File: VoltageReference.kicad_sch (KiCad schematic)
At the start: 1 part

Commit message: finish some unconnect pins, draw edge cut board
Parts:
- RV2: footprint IVS_FOOTPRINTS:Potentiometer_Bourns_TC33X_Vertical -> SpiritBoi_Footprint_Library:Potentiometer-Vert-SMD-3P-Bourns_TC33X
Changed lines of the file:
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@@
 			)
 		)
-		(property "Footprint" "IVS_FOOTPRINTS:Potentiometer_Bourns_TC33X_Vertical"
+		(property "Footprint" "SpiritBoi_Footprint_Library:Potentiometer-Vert-SMD-3P-Bourns_TC33X"
 			(at 81.915 95.25 0)
 			(effects

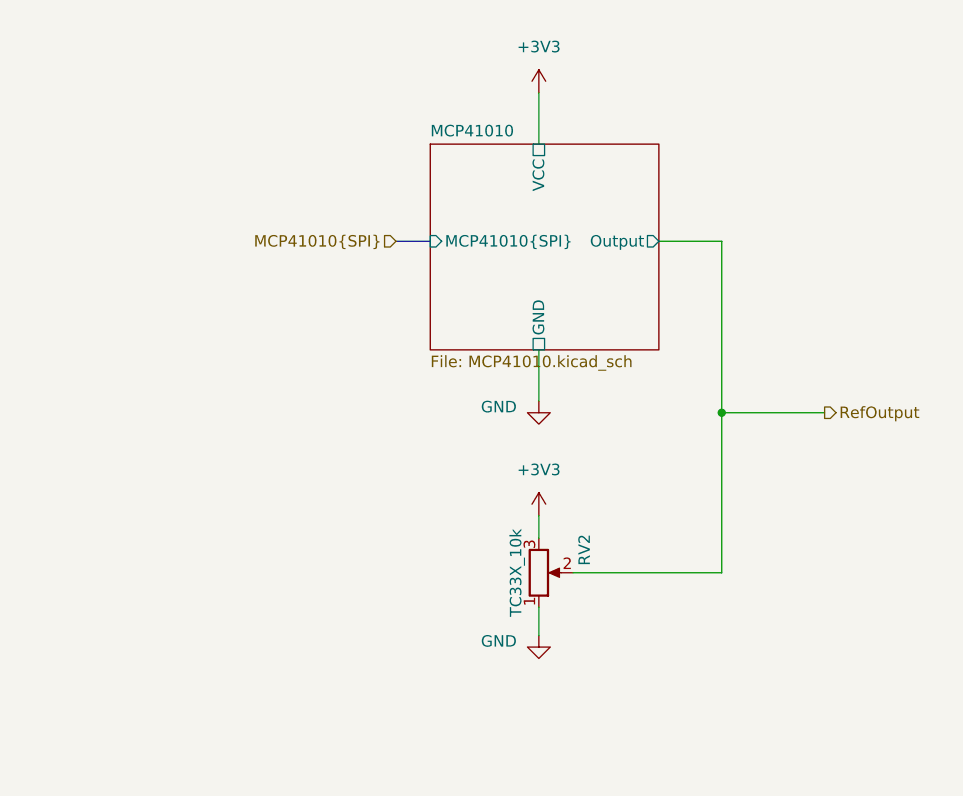
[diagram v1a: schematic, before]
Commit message: Add LORA, SDcard and Volt to 4_20mA scheamtic
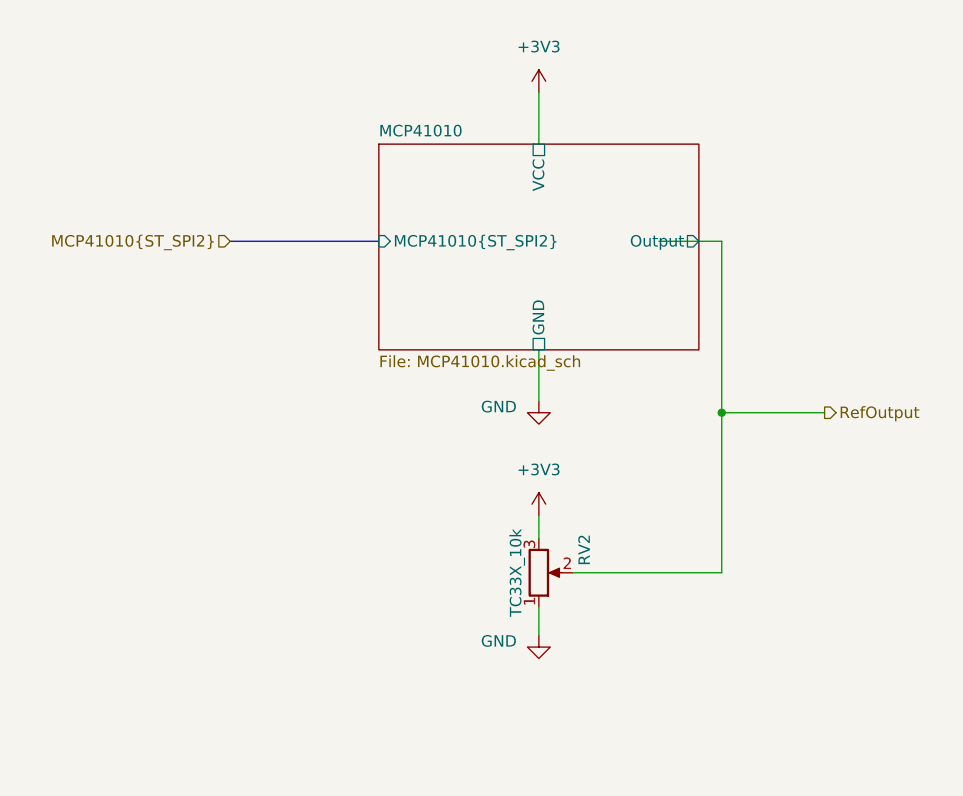
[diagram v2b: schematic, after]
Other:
- sheet MCP41010 ports: added MCP41010{ST_SPI2}; removed MCP41010{SPI}
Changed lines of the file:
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@@
 	(bus
 		(pts
-			(xy 66.04 58.42) (xy 69.85 58.42)
+			(xy 47.625 58.42) (xy 64.135 58.42)
 		)
 		(stroke
@@
 		)
 	)
-	(hierarchical_label "MCP41010{SPI}"
+	(hierarchical_label "MCP41010{ST_SPI2}"
 		(shape input)
-		(at 66.04 58.42 180)
+		(at 47.625 58.42 180)
 		(fields_autoplaced yes)
 		(effects
@@
 		(on_board yes)
 		(dnp no)
-		(property "Reference" "#PWR0141"
+		(property "Reference" "#PWR0112"
 			(at 81.915 108.585 0)
 			(effects
@@
 			(project "DongTamV2"
 				(path "/2303d546-b88a-4ab0-aee1-26e3b32ac9d7/c44414d4-f62b-4b90-ad16-4c8725291991"
-					(reference "#PWR0141")
+					(reference "#PWR0112")
 					(unit 1)
 				)
@@
 		(dnp no)
 		(fields_autoplaced yes)
-		(property "Reference" "#PWR0140"
+		(property "Reference" "#PWR0111"
 			(at 81.915 92.71 0)
 			(effects
@@
 			(project "DongTamV2"
 				(path "/2303d546-b88a-4ab0-aee1-26e3b32ac9d7/c44414d4-f62b-4b90-ad16-4c8725291991"
-					(reference "#PWR0140")
+					(reference "#PWR0111")
 					(unit 1)
 				)
@@
 		(on_board yes)
 		(dnp no)
-		(property "Reference" "#PWR0121"
+		(property "Reference" "#PWR0110"
 			(at 81.915 82.55 0)
 			(effects
@@
 			(project "DongTamV2"
 				(path "/2303d546-b88a-4ab0-aee1-26e3b32ac9d7/c44414d4-f62b-4b90-ad16-4c8725291991"
-					(reference "#PWR0121")
+					(reference "#PWR0110")
 					(unit 1)
 				)
@@
 		(dnp no)
 		(fields_autoplaced yes)
-		(property "Reference" "#PWR0122"
+		(property "Reference" "#PWR0109"
 			(at 81.915 45.72 0)
 			(effects
@@
 			(project "DongTamV2"
 				(path "/2303d546-b88a-4ab0-aee1-26e3b32ac9d7/c44414d4-f62b-4b90-ad16-4c8725291991"
-					(reference "#PWR0122")
+					(reference "#PWR0109")
 					(unit 1)
 				)
@@
 	)
 	(sheet
-		(at 69.85 47.625)
-		(size 25.4 22.86)
+		(at 64.135 47.625)
+		(size 35.56 22.86)
 		(fields_autoplaced yes)
 		(stroke
@@
 		)
 		(property "Sheetname" "MCP41010"
-			(at 69.85 46.9134 0)
+			(at 64.135 46.9134 0)
 			(effects
 				(font
@@
 		)
 		(property "Sheetfile" "MCP41010.kicad_sch"
-			(at 69.85 71.0696 0)
+			(at 64.135 71.0696 0)
 			(effects
 				(font
@@
 		)
 		(pin "Output" output
-			(at 95.25 58.42 0)
+			(at 99.695 58.42 0)
 			(effects
 				(font
@@
 			)
 		)
-		(pin "MCP41010{SPI}" input
-			(at 69.85 58.42 180)
-			(effects
-				(font
+		(pin "MCP41010{ST_SPI2}" input
+			(at 64.135 58.42 180)
+			(effects
+				(font

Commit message: layout p1
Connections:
- net +3V3 renamed +3.3V
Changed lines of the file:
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@@
+	)
+	(symbol
+		(lib_id "power:+3.3V")
+		(at 81.915 88.9 0)
+		(unit 1)
+		(exclude_from_sim no)
+		(in_bom yes)
+		(on_board yes)
+		(dnp no)
+		(fields_autoplaced yes)
+		(property "Reference" "#PWR0109"
+			(at 81.915 92.71 0)
+			(effects
+				(font
+					(size 1.27 1.27)
+				)
+				(hide yes)
+			)
+		)
+		(property "Value" "+3.3V"
+			(at 81.915 83.82 0)
+			(effects
+				(font
+					(size 1.27 1.27)
+				)
+			)
+		)
+		(property "Footprint" ""
+			(at 81.915 88.9 0)
+			(effects
+				(font
+					(size 1.27 1.27)
+				)
+				(hide yes)
+			)
+		)
+		(property "Datasheet" ""
+			(at 81.915 88.9 0)
+			(effects
+				(font
+					(size 1.27 1.27)
+				)
+				(hide yes)
+			)
+		)
+		(property "Description" "Power symbol creates a global label with name \"+3.3V\""
+			(at 81.915 88.9 0)
+			(effects
+				(font
+					(size 1.27 1.27)
+				)
+				(hide yes)
+			)
+		)
+		(pin "1"
+		)
+		(instances
+			(project "DongTamV2"
+				(path "/2303d546-b88a-4ab0-aee1-26e3b32ac9d7/c44414d4-f62b-4b90-ad16-4c8725291991"
+					(reference "#PWR0109")
+					(unit 1)
+				)
+			)
+		)
 	)
 	(symbol
@@
 	)
 	(symbol
-		(lib_id "power:+3V3")
-		(at 81.915 88.9 0)
-		(mirror y)
-		(unit 1)
-		(exclude_from_sim no)
-		(in_bom yes)
-		(on_board yes)
-		(dnp no)
-		(fields_autoplaced yes)
-		(property "Reference" "#PWR0111"
-			(at 81.915 92.71 0)
-			(effects
-				(font
-					(size 1.27 1.27)
-				)
-				(hide yes)
-			)
-		)
-		(property "Value" "+3V3"
-			(at 81.915 83.82 0)
-			(effects
-				(font
-					(size 1.27 1.27)
-				)
-			)
-		)
-		(property "Footprint" ""
-			(at 81.915 88.9 0)
-			(effects
-				(font
-					(size 1.27 1.27)
-				)
-				(hide yes)
-			)
-		)
-		(property "Datasheet" ""
-			(at 81.915 88.9 0)
-			(effects
-				(font
-					(size 1.27 1.27)
-				)
-				(hide yes)
-			)
-		)
-		(property "Description" ""
-			(at 81.915 88.9 0)
-			(effects
-				(font
-					(size 1.27 1.27)
-				)
-				(hide yes)
-			)
-		)
-		(pin "1"
-		)
-		(instances
-			(project "DongTamV2"
-				(path "/2303d546-b88a-4ab0-aee1-26e3b32ac9d7/c44414d4-f62b-4b90-ad16-4c8725291991"
-					(reference "#PWR0111")
-					(unit 1)
-				)
-			)
-		)
-	)
-	(symbol
 		(lib_id "power:GND")
 		(at 81.915 76.2 0)
@@
 	)
 	(symbol
+		(lib_id "power:+3.3V")
+		(at 81.915 41.91 0)
+		(unit 1)
+		(exclude_from_sim no)
+		(in_bom yes)
+		(on_board yes)
+		(dnp no)
+		(fields_autoplaced yes)
+		(property "Reference" "#PWR048"
+			(at 81.915 45.72 0)
+			(effects
+				(font
+					(size 1.27 1.27)
+				)
+				(hide yes)
+			)
+		)
+		(property "Value" "+3.3V"
+			(at 81.915 36.83 0)
+			(effects
+				(font
+					(size 1.27 1.27)
+				)
+			)
+		)
+		(property "Footprint" ""
+			(at 81.915 41.91 0)
+			(effects
+				(font
+					(size 1.27 1.27)
+				)
+				(hide yes)
+			)
+		)
+		(property "Datasheet" ""
+			(at 81.915 41.91 0)
+			(effects
+				(font
+					(size 1.27 1.27)
+				)
+				(hide yes)
+			)
+		)
+		(property "Description" "Power symbol creates a global label with name \"+3.3V\""
+			(at 81.915 41.91 0)
+			(effects
+				(font
+					(size 1.27 1.27)
+				)
+				(hide yes)
+			)
+		)
+		(pin "1"
+		)
+		(instances
+			(project "DongTamV2"
+				(path "/2303d546-b88a-4ab0-aee1-26e3b32ac9d7/c44414d4-f62b-4b90-ad16-4c8725291991"
+					(reference "#PWR048")
+					(unit 1)
+				)
+			)
+		)
+	)
+	(symbol
 		(lib_id "Device:R_Potentiometer")
 		(at 81.915 95.25 0)
@@
 					(unit 1)
 				)
-			)
-		)
-	)
-	(symbol
-		(lib_id "power:+3V3")
-		(at 81.915 41.91 0)
-		(mirror y)
-		(unit 1)
-		(exclude_from_sim no)
-		(in_bom yes)
-		(on_board yes)
-		(dnp no)
-		(fields_autoplaced yes)
-		(property "Reference" "#PWR0109"
-			(at 81.915 45.72 0)
-			(effects
-				(font
-					(size 1.27 1.27)
-				)
-				(hide yes)
-			)
-		)
-		(property "Value" "+3V3"
-			(at 81.915 36.83 0)
-			(effects
-				(font
-					(size 1.27 1.27)
-				)
-			)
-		)
-		(property "Footprint" ""
-			(at 81.915 41.91 0)
-			(effects
-				(font
-					(size 1.27 1.27)
-				)
-				(hide yes)
-			)
-		)
-		(property "Datasheet" ""
-			(at 81.915 41.91 0)
-			(effects
-				(font
-					(size 1.27 1.27)
-				)
-				(hide yes)
-			)
-		)
-		(property "Description" ""
-			(at 81.915 41.91 0)
-			(effects
-				(font
-					(size 1.27 1.27)
-				)
-				(hide yes)
-			)
-		)
-		(pin "1"
-		)
-		(instances
-			(project "DongTamV2"
-				(path "/2303d546-b88a-4ab0-aee1-26e3b32ac9d7/c44414d4-f62b-4b90-ad16-4c8725291991"
-					(reference "#PWR0109")
-					(unit 1)
-				)

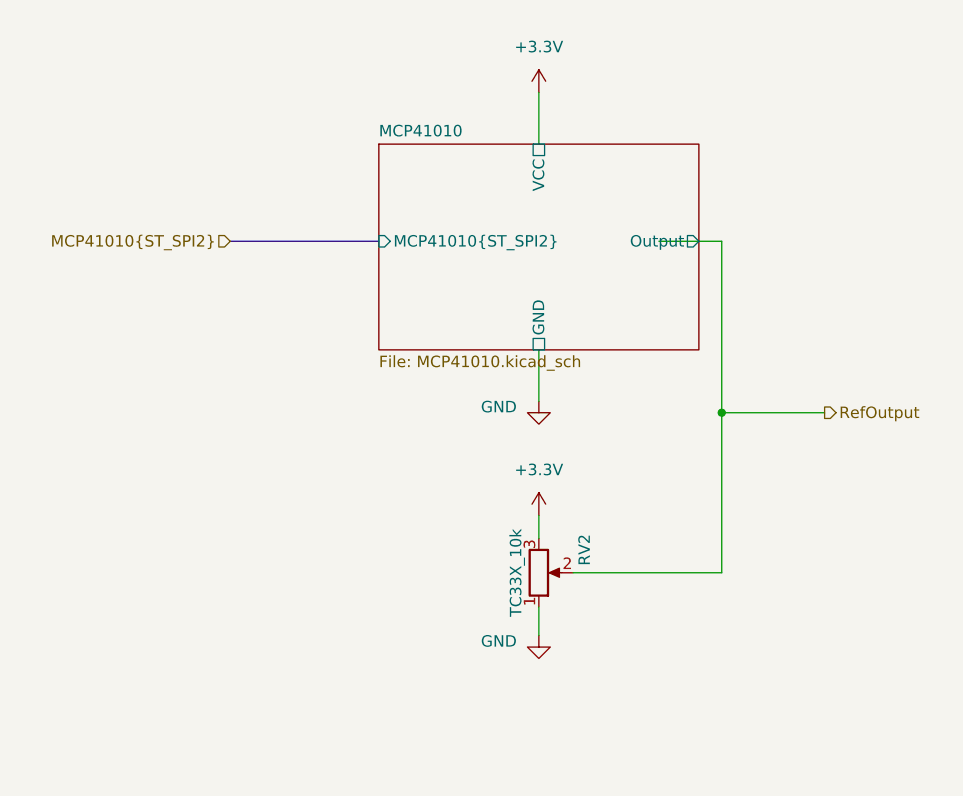
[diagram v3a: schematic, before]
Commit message: Layout p2, fix Analog VCC and GND for opamp circuit
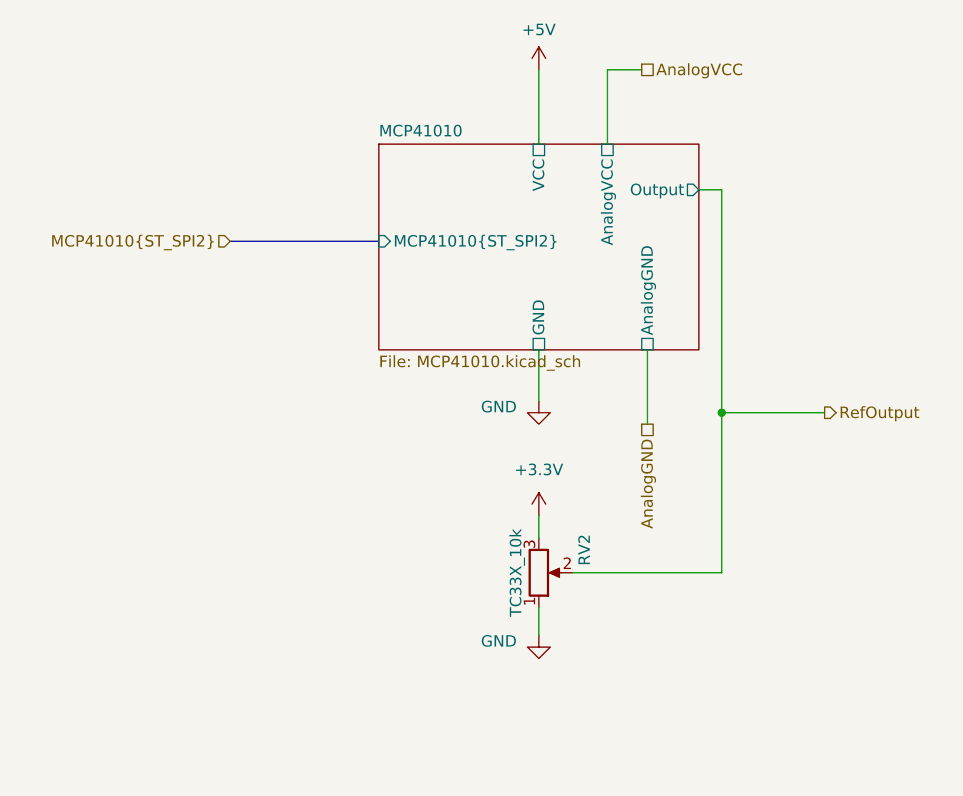
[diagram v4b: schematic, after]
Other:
- sheet MCP41010 ports: added AnalogGND, AnalogVCC; removed none
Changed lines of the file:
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@@
+	(wire
+		(pts
+			(xy 81.915 39.37) (xy 81.915 47.625)
+		)
+		(stroke
+			(width 0)
+			(type default)
+		)
+	)
 	(wire
 		(pts
@@
 	(wire
 		(pts
-			(xy 102.235 77.47) (xy 102.235 58.42)
+			(xy 102.235 77.47) (xy 102.235 52.705)
 		)
 		(stroke
@@
 	(wire
 		(pts
-			(xy 102.235 58.42) (xy 95.25 58.42)
+			(xy 93.345 39.37) (xy 89.535 39.37)
 		)
 		(stroke
@@
 	(wire
 		(pts
+			(xy 89.535 39.37) (xy 89.535 47.625)
+		)
+		(stroke
+			(width 0)
+			(type default)
+		)
+	)
+	(wire
+		(pts
+			(xy 99.695 52.705) (xy 102.235 52.705)
+		)
+		(stroke
+			(width 0)
+			(type default)
+		)
+	)
+	(wire
+		(pts
 			(xy 81.915 91.44) (xy 81.915 88.9)
 		)
@@
 	(wire
 		(pts
-			(xy 81.915 41.91) (xy 81.915 47.625)
+			(xy 93.98 70.485) (xy 93.98 78.74)
 		)
 		(stroke
@@
 			(width 0)
 			(type default)
+		)
+	)
+	(hierarchical_label "AnalogGND"
+		(shape passive)
+		(at 93.98 78.74 270)
+		(fields_autoplaced yes)
+		(effects
+			(font
+				(size 1.27 1.27)
+			)
+			(justify right)
+		)
+	)
+	(hierarchical_label "AnalogVCC"
+		(shape passive)
+		(at 93.345 39.37 0)
+		(fields_autoplaced yes)
+		(effects
+			(font
+				(size 1.27 1.27)
+			)
+			(justify left)
 		)
 	)
@@
 	)
 	(symbol
-		(lib_id "power:+3.3V")
-		(at 81.915 41.91 0)
+		(lib_id "power:+5V")
+		(at 81.915 39.37 0)
 		(unit 1)
 		(exclude_from_sim no)
@@
 		(dnp no)
 		(fields_autoplaced yes)
-		(property "Reference" "#PWR048"
-			(at 81.915 45.72 0)
-			(effects
-				(font
-					(size 1.27 1.27)
-				)
-				(hide yes)
-			)
-		)
-		(property "Value" "+3.3V"
-			(at 81.915 36.83 0)
+		(property "Reference" "#PWR052"
+			(at 81.915 43.18 0)
+			(effects
+				(font
+					(size 1.27 1.27)
+				)
+				(hide yes)
+			)
+		)
+		(property "Value" "+5V"
+			(at 81.915 34.925 0)
 			(effects
 				(font
@@
 		)
 		(property "Footprint" ""
-			(at 81.915 41.91 0)
+			(at 81.915 39.37 0)
 			(effects
 				(font
@@
 		)
 		(property "Datasheet" ""
-			(at 81.915 41.91 0)
-			(effects
-				(font
-					(size 1.27 1.27)
-				)
-				(hide yes)
-			)
-		)
-		(property "Description" "Power symbol creates a global label with name \"+3.3V\""
-			(at 81.915 41.91 0)
+			(at 81.915 39.37 0)
+			(effects
+				(font
+					(size 1.27 1.27)
+				)
+				(hide yes)
+			)
+		)
+		(property "Description" "Power symbol creates a global label with name \"+5V\""
+			(at 81.915 39.37 0)
 			(effects
 				(font
@@
 			(project "DongTamV2"
 				(path "/2303d546-b88a-4ab0-aee1-26e3b32ac9d7/c44414d4-f62b-4b90-ad16-4c8725291991"
-					(reference "#PWR048")
+					(reference "#PWR052")
 					(unit 1)
 				)
@@
 		)
 		(pin "Output" output
-			(at 99.695 58.42 0)
+			(at 99.695 52.705 0)
 			(effects
 				(font
@@
 			)
 		)
+		(pin "AnalogGND" passive
+			(at 93.98 70.485 270)
+			(effects
+				(font
+					(size 1.27 1.27)
+				)
+				(justify left)
+			)
+		)
+		(pin "AnalogVCC" passive
+			(at 89.535 47.625 90)
+			(effects
+				(font
+					(size 1.27 1.27)
+				)
+				(justify right)
+			)
+		)

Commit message: Complete layout, HW685 not layout yet
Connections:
- net +3.3V is gone; now on net AnalogVCC: RV2.3
- net AnalogGND: now also RV2.1
- net GND: no longer RV2.1
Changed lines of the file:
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@@
 	(wire
 		(pts
-			(xy 81.915 99.06) (xy 81.915 102.235)
+			(xy 81.915 99.06) (xy 81.915 104.14)
 		)
 		(stroke
@@
 	(wire
 		(pts
-			(xy 81.915 91.44) (xy 81.915 88.9)
+			(xy 81.915 85.725) (xy 81.915 91.44)
 		)
 		(stroke
@@
 		)
 	)
+	(wire
+		(pts
+			(xy 75.565 85.725) (xy 81.915 85.725)
+		)
+		(stroke
+			(width 0)
+			(type default)
+		)
+	)
+	(hierarchical_label "AnalogGND"
+		(shape passive)
+		(at 81.915 104.14 270)
+		(fields_autoplaced yes)
+		(effects
+			(font
+				(size 1.27 1.27)
+			)
+			(justify right)
+		)
+	)
 	(hierarchical_label "AnalogGND"
 		(shape passive)
@@
 			)
 			(justify left)
+		)
+	)
+	(hierarchical_label "AnalogVCC"
+		(shape passive)
+		(at 75.565 85.725 180)
+		(fields_autoplaced yes)
+		(effects
+			(font
+				(size 1.27 1.27)
+			)
+			(justify right)
 		)
 	)
@@
 		)
 	)
-	(symbol
-		(lib_id "power:+3.3V")
-		(at 81.915 88.9 0)
-		(unit 1)
-		(exclude_from_sim no)
-		(in_bom yes)
-		(on_board yes)
-		(dnp no)
-		(fields_autoplaced yes)
-		(property "Reference" "#PWR0109"
-			(at 81.915 92.71 0)
-			(effects
-				(font
-					(size 1.27 1.27)
-				)
-				(hide yes)
-			)
-		)
-		(property "Value" "+3.3V"
-			(at 81.915 83.82 0)
-			(effects
-				(font
-					(size 1.27 1.27)
-				)
-			)
-		)
-		(property "Footprint" ""
-			(at 81.915 88.9 0)
-			(effects
-				(font
-					(size 1.27 1.27)
-				)
-				(hide yes)
-			)
-		)
-		(property "Datasheet" ""
-			(at 81.915 88.9 0)
-			(effects
-				(font
-					(size 1.27 1.27)
-				)
-				(hide yes)
-			)
-		)
-		(property "Description" "Power symbol creates a global label with name \"+3.3V\""
-			(at 81.915 88.9 0)
-			(effects
-				(font
-					(size 1.27 1.27)
-				)
-				(hide yes)
-			)
-		)
-		(pin "1"
-		)
-		(instances
-			(project "DongTamV2"
-				(path "/2303d546-b88a-4ab0-aee1-26e3b32ac9d7/c44414d4-f62b-4b90-ad16-4c8725291991"
-					(reference "#PWR0109")
-					(unit 1)
-				)
-			)
-		)
-	)
-	(symbol
-		(lib_id "power:GND")
-		(at 81.915 102.235 0)
-		(mirror y)
-		(unit 1)
-		(exclude_from_sim no)
-		(in_bom yes)
-		(on_board yes)
-		(dnp no)
-		(property "Reference" "#PWR0112"
-			(at 81.915 108.585 0)
-			(effects
-				(font
-					(size 1.27 1.27)
-				)
-				(hide yes)
-			)
-		)
-		(property "Value" "GND"
-			(at 77.47 102.87 0)
-			(effects
-				(font
-					(size 1.27 1.27)
-				)
-			)
-		)
-		(property "Footprint" ""
-			(at 81.915 102.235 0)
-			(effects
-				(font
-					(size 1.27 1.27)
-				)
-				(hide yes)
-			)
-		)
-		(property "Datasheet" ""
-			(at 81.915 102.235 0)
-			(effects
-				(font
-					(size 1.27 1.27)
-				)
-				(hide yes)
-			)
-		)
-		(property "Description" ""
-			(at 81.915 102.235 0)
-			(effects
-				(font
-					(size 1.27 1.27)
-				)
-				(hide yes)
-			)
-		)
-		(pin "1"
-		)
-		(instances
-			(project "DongTamV2"
-				(path "/2303d546-b88a-4ab0-aee1-26e3b32ac9d7/c44414d4-f62b-4b90-ad16-4c8725291991"
-					(reference "#PWR0112")
-					(unit 1)
-				)
-			)
-		)
-	)
